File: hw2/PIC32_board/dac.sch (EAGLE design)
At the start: 1 part

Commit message: Edit pin label
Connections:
- net B8/SDI1 renamed A1/SDO1
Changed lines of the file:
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@@
 </segment>
 </net>
-<net name="B8/SDI1" class="0">
+<net name="A1/SDO1" class="0">
 <segment>
 <pinref part="DAC" gate="G$1" pin="5.SDI"/>

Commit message: Add expander chip to schematic library
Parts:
- added 330: (no value), me433:R-US_R0603
- added BUTTON: PUSH, me433:PUSH
- added EXPANDER: MCP23008, me433:MCP23008
- added LED: YELLOW, me433:LED-RED0603
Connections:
- removed net 3.3V: DAC.11.VREFB, DAC.13.VREFA
- new net B2/SDA2: EXPANDER.2.SDA
- new net B3/SCL2: EXPANDER.1.SCL
- new net MCLR: EXPANDER.6.RESET
- new net N$1: EXPANDER.10.GP0, LED.A
- new net N$2: BUTTON.1, EXPANDER.17.GP7
- new net N$3: EXPANDER.3.A2
- new net N$4: EXPANDER.4.A1
- new net N$5: EXPANDER.5.A0
- new net N$6: 330.1, LED.C
- net +3V3: now also DAC.11.VREFB, DAC.13.VREFA, EXPANDER.18.VDD
- net GND: now also 330.2, BUTTON.2, EXPANDER.9.VSS
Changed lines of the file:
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@@
 <part name="GND1" library="me433" deviceset="GND" device=""/>
 <part name="+3V1" library="me433" deviceset="+3V3" device=""/>
+<part name="EXPANDER" library="me433" deviceset="MCP23008" device=""/>
+<part name="+3V2" library="me433" deviceset="+3V3" device=""/>
+<part name="GND2" library="me433" deviceset="GND" device=""/>
+<part name="LED" library="me433" deviceset="LED-RED" device="0603" value="YELLOW"/>
+<part name="GND3" library="me433" deviceset="GND" device=""/>
+<part name="BUTTON" library="me433" deviceset="PUSH" device=""/>
+<part name="GND4" library="me433" deviceset="GND" device=""/>
+<part name="330" library="me433" deviceset="R-US_" device="R0603" package3d_urn="urn:adsk.eagle:package:26057/1"/>
 </parts>
 <sheets>
@@
 <instance part="DAC" gate="G$1" x="-2.54" y="0"/>
 <instance part="GND1" gate="1" x="33.02" y="-20.32"/>
-<instance part="+3V1" gate="G$1" x="-35.56" y="20.32"/>
+<instance part="+3V1" gate="G$1" x="-33.02" y="20.32"/>
 </instances>
 <busses>
 </busses>
 <nets>
-<net name="3.3V" class="0">
-<segment>
-<pinref part="DAC" gate="G$1" pin="13.VREFA"/>
-<wire x1="17.78" y1="10.16" x2="30.48" y2="10.16" width="0.1524" layer="91"/>
-<label x="25.4" y="10.16" size="1.778" layer="95"/>
-</segment>
-<segment>
-<pinref part="DAC" gate="G$1" pin="11.VREFB"/>
-<wire x1="17.78" y1="0" x2="30.48" y2="0" width="0.1524" layer="91"/>
-<label x="25.4" y="0" size="1.778" layer="95"/>
-</segment>
-</net>
 <net name="A0/SS1" class="0">
 <segment>
@@
 <segment>
 <pinref part="DAC" gate="G$1" pin="1.VDD"/>
-<wire x1="-17.78" y1="15.24" x2="-35.56" y2="15.24" width="0.1524" layer="91"/>
-<label x="-33.02" y="15.24" size="1.778" layer="95"/>
+<wire x1="-17.78" y1="15.24" x2="-33.02" y2="15.24" width="0.1524" layer="91"/>
 <pinref part="+3V1" gate="G$1" pin="+3V3"/>
-<wire x1="-35.56" y1="15.24" x2="-35.56" y2="17.78" width="0.1524" layer="91"/>
+<wire x1="-33.02" y1="15.24" x2="-33.02" y2="17.78" width="0.1524" layer="91"/>
+</segment>
+<segment>
+<pinref part="DAC" gate="G$1" pin="13.VREFA"/>
+<wire x1="17.78" y1="10.16" x2="30.48" y2="10.16" width="0.1524" layer="91"/>
+<label x="25.4" y="10.16" size="1.778" layer="95"/>
+</segment>
+<segment>
+<pinref part="DAC" gate="G$1" pin="11.VREFB"/>
+<wire x1="17.78" y1="0" x2="30.48" y2="0" width="0.1524" layer="91"/>
+<label x="25.4" y="0" size="1.778" layer="95"/>
+</segment>
+</net>
+</nets>
+</sheet>
+<sheet>
+<plain>
+</plain>
+<instances>
+<instance part="EXPANDER" gate="G$1" x="0" y="0"/>
+<instance part="+3V2" gate="G$1" x="27.94" y="20.32"/>
+<instance part="GND2" gate="1" x="-27.94" y="-33.02"/>
+<instance part="LED" gate="G$1" x="27.94" y="-25.4" rot="R90"/>
+<instance part="GND3" gate="1" x="48.26" y="-27.94"/>
+<instance part="BUTTON" gate="G$1" x="35.56" y="0" rot="R270"/>
+<instance part="GND4" gate="1" x="35.56" y="-15.24"/>
+<instance part="330" gate="G$1" x="40.64" y="-25.4"/>
+</instances>
+<busses>
+</busses>
+<nets>
+<net name="B3/SCL2" class="0">
+<segment>
+<pinref part="EXPANDER" gate="G$1" pin="1.SCL"/>
+<wire x1="-15.24" y1="15.24" x2="-27.94" y2="15.24" width="0.1524" layer="91"/>
+<label x="-27.94" y="15.24" size="1.778" layer="95"/>
+</segment>
+</net>
+<net name="B2/SDA2" class="0">
+<segment>
+<pinref part="EXPANDER" gate="G$1" pin="2.SDA"/>
+<wire x1="-15.24" y1="10.16" x2="-27.94" y2="10.16" width="0.1524" layer="91"/>
+<label x="-27.94" y="10.16" size="1.778" layer="95"/>
+</segment>
+</net>
+<net name="N$3" class="0">
+<segment>
+<pinref part="EXPANDER" gate="G$1" pin="3.A2"/>
+<wire x1="-15.24" y1="5.08" x2="-27.94" y2="5.08" width="0.1524" layer="91"/>
+</segment>
+</net>
+<net name="N$4" class="0">
+<segment>
+<pinref part="EXPANDER" gate="G$1" pin="4.A1"/>
+<wire x1="-15.24" y1="0" x2="-27.94" y2="0" width="0.1524" layer="91"/>
+</segment>
+</net>
+<net name="N$5" class="0">
+<segment>
+<pinref part="EXPANDER" gate="G$1" pin="5.A0"/>
+<wire x1="-15.24" y1="-5.08" x2="-27.94" y2="-5.08" width="0.1524" layer="91"/>
+</segment>
+</net>
+<net name="MCLR" class="0">
+<segment>
+<pinref part="EXPANDER" gate="G$1" pin="6.RESET"/>
+<wire x1="-15.24" y1="-10.16" x2="-27.94" y2="-10.16" width="0.1524" layer="91"/>
+<label x="-27.94" y="-10.16" size="1.778" layer="95"/>
+</segment>
+</net>
+<net name="+3V3" class="0">
+<segment>
+<pinref part="EXPANDER" gate="G$1" pin="18.VDD"/>
+<wire x1="17.78" y1="15.24" x2="27.94" y2="15.24" width="0.1524" layer="91"/>
+<pinref part="+3V2" gate="G$1" pin="+3V3"/>
+<wire x1="27.94" y1="15.24" x2="27.94" y2="17.78" width="0.1524" layer="91"/>
+</segment>
+</net>
+<net name="GND" class="0">
+<segment>
+<pinref part="EXPANDER" gate="G$1" pin="9.VSS"/>
+<wire x1="-15.24" y1="-25.4" x2="-27.94" y2="-25.4" width="0.1524" layer="91"/>
+<pinref part="GND2" gate="1" pin="GND"/>
+<wire x1="-27.94" y1="-30.48" x2="-27.94" y2="-25.4" width="0.1524" layer="91"/>
+</segment>
+<segment>
+<pinref part="BUTTON" gate="G$1" pin="2"/>
+<pinref part="GND4" gate="1" pin="GND"/>
+<wire x1="35.56" y1="-10.16" x2="35.56" y2="-12.7" width="0.1524" layer="91"/>
+</segment>
+<segment>
+<pinref part="330" gate="G$1" pin="2"/>
+<pinref part="GND3" gate="1" pin="GND"/>
+<wire x1="45.72" y1="-25.4" x2="48.26" y2="-25.4" width="0.1524" layer="91"/>
+</segment>
+</net>
+<net name="N$1" class="0">
+<segment>
+<pinref part="EXPANDER" gate="G$1" pin="10.GP0"/>
+<pinref part="LED" gate="G$1" pin="A"/>
+<wire x1="17.78" y1="-25.4" x2="25.4" y2="-25.4" width="0.1524" layer="91"/>
+</segment>
+</net>
+<net name="N$2" class="0">
+<segment>
+<pinref part="EXPANDER" gate="G$1" pin="17.GP7"/>
+<pinref part="BUTTON" gate="G$1" pin="1"/>
+<wire x1="17.78" y1="10.16" x2="35.56" y2="10.16" width="0.1524" layer="91"/>
+</segment>
+</net>
+<net name="N$6" class="0">
+<segment>
+<pinref part="LED" gate="G$1" pin="C"/>
+<pinref part="330" gate="G$1" pin="1"/>
+<wire x1="33.02" y1="-25.4" x2="35.56" y2="-25.4" width="0.1524" layer="91"/>
 </segment>
 </net>
@@
 </schematic>
 </drawing>
+<compatibility>
+<note version="8.3" severity="warning">
+Since Version 8.3, EAGLE supports URNs for individual library
+assets (packages, symbols, and devices). The URNs of those assets
+will not be understood (or retained) with this version.
+</note>
+<note version="8.3" severity="warning">
+Since Version 8.3, EAGLE supports the association of 3D packages
+with devices in libraries, schematics, and board files. Those 3D
+packages will not be understood (or retained) with this version.
+</note>
+</compatibility>
 </eagle>

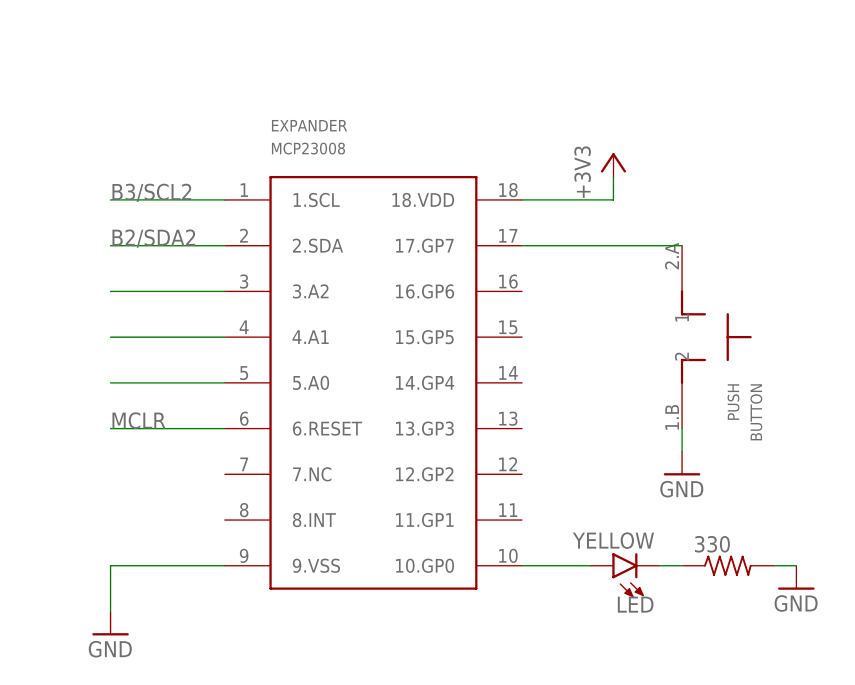
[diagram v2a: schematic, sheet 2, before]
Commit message: Edit schematic labels
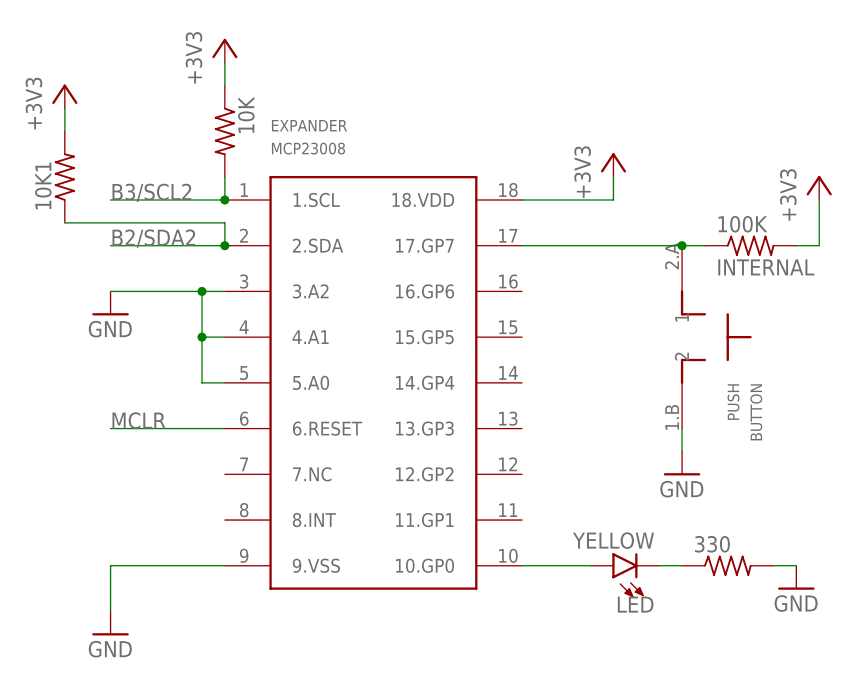
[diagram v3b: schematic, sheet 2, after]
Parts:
- added 100K: INTERNAL, me433:R-US_R0603
- added 10K, 10K1: (no value), me433:R-US_R0603
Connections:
- removed net N$3: EXPANDER.3.A2
- removed net N$4: EXPANDER.4.A1
- removed net N$5: EXPANDER.5.A0
- net +3V3: now also 100K.2, 10K.1, 10K1.2
- net B2/SDA2: now also 10K1.1
- net B3/SCL2: now also 10K.2
- net GND: now also EXPANDER.3.A2, EXPANDER.4.A1, EXPANDER.5.A0
- net N$2: now also 100K.1
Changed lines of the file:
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@@
 <part name="GND4" library="me433" deviceset="GND" device=""/>
 <part name="330" library="me433" deviceset="R-US_" device="R0603" package3d_urn="urn:adsk.eagle:package:26057/1"/>
+<part name="100K" library="me433" deviceset="R-US_" device="R0603" package3d_urn="urn:adsk.eagle:package:26057/1" value="INTERNAL"/>
+<part name="GND5" library="me433" deviceset="GND" device=""/>
+<part name="+3V3" library="me433" deviceset="+3V3" device=""/>
+<part name="10K" library="me433" deviceset="R-US_" device="R0603" package3d_urn="urn:adsk.eagle:package:26057/1"/>
+<part name="10K1" library="me433" deviceset="R-US_" device="R0603" package3d_urn="urn:adsk.eagle:package:26057/1"/>
+<part name="+3V4" library="me433" deviceset="+3V3" device=""/>
+<part name="+3V5" library="me433" deviceset="+3V3" device=""/>
 </parts>
 <sheets>
@@
 <instance part="GND4" gate="1" x="35.56" y="-15.24"/>
 <instance part="330" gate="G$1" x="40.64" y="-25.4"/>
+<instance part="100K" gate="G$1" x="43.18" y="10.16"/>
+<instance part="GND5" gate="1" x="-27.94" y="2.54"/>
+<instance part="+3V3" gate="G$1" x="50.8" y="17.78"/>
+<instance part="10K" gate="G$1" x="-15.24" y="22.86" rot="R270"/>
+<instance part="10K1" gate="G$1" x="-33.02" y="17.78" rot="R90"/>
+<instance part="+3V4" gate="G$1" x="-15.24" y="33.02"/>
+<instance part="+3V5" gate="G$1" x="-33.02" y="27.94"/>
 </instances>
 <busses>
@@
 <wire x1="-15.24" y1="15.24" x2="-27.94" y2="15.24" width="0.1524" layer="91"/>
 <label x="-27.94" y="15.24" size="1.778" layer="95"/>
+<pinref part="10K" gate="G$1" pin="2"/>
+<wire x1="-15.24" y1="15.24" x2="-15.24" y2="17.78" width="0.1524" layer="91"/>
+<junction x="-15.24" y="15.24"/>
 </segment>
 </net>
@@
 <wire x1="-15.24" y1="10.16" x2="-27.94" y2="10.16" width="0.1524" layer="91"/>
 <label x="-27.94" y="10.16" size="1.778" layer="95"/>
-</segment>
-</net>
-<net name="N$3" class="0">
-<segment>
-<pinref part="EXPANDER" gate="G$1" pin="3.A2"/>
-<wire x1="-15.24" y1="5.08" x2="-27.94" y2="5.08" width="0.1524" layer="91"/>
-</segment>
-</net>
-<net name="N$4" class="0">
-<segment>
-<pinref part="EXPANDER" gate="G$1" pin="4.A1"/>
-<wire x1="-15.24" y1="0" x2="-27.94" y2="0" width="0.1524" layer="91"/>
-</segment>
-</net>
-<net name="N$5" class="0">
-<segment>
-<pinref part="EXPANDER" gate="G$1" pin="5.A0"/>
-<wire x1="-15.24" y1="-5.08" x2="-27.94" y2="-5.08" width="0.1524" layer="91"/>
+<wire x1="-15.24" y1="10.16" x2="-15.24" y2="12.7" width="0.1524" layer="91"/>
+<junction x="-15.24" y="10.16"/>
+<pinref part="10K1" gate="G$1" pin="1"/>
+<wire x1="-15.24" y1="12.7" x2="-33.02" y2="12.7" width="0.1524" layer="91"/>
 </segment>
 </net>
@@
 <wire x1="27.94" y1="15.24" x2="27.94" y2="17.78" width="0.1524" layer="91"/>
 </segment>
+<segment>
+<pinref part="100K" gate="G$1" pin="2"/>
+<pinref part="+3V3" gate="G$1" pin="+3V3"/>
+<wire x1="48.26" y1="10.16" x2="50.8" y2="10.16" width="0.1524" layer="91"/>
+<wire x1="50.8" y1="10.16" x2="50.8" y2="15.24" width="0.1524" layer="91"/>
+</segment>
+<segment>
+<pinref part="10K1" gate="G$1" pin="2"/>
+<pinref part="+3V5" gate="G$1" pin="+3V3"/>
+<wire x1="-33.02" y1="22.86" x2="-33.02" y2="25.4" width="0.1524" layer="91"/>
+</segment>
+<segment>
+<pinref part="10K" gate="G$1" pin="1"/>
+<pinref part="+3V4" gate="G$1" pin="+3V3"/>
+<wire x1="-15.24" y1="27.94" x2="-15.24" y2="30.48" width="0.1524" layer="91"/>
+</segment>
 </net>
 <net name="GND" class="0">
@@
 <wire x1="45.72" y1="-25.4" x2="48.26" y2="-25.4" width="0.1524" layer="91"/>
 </segment>
+<segment>
+<pinref part="EXPANDER" gate="G$1" pin="3.A2"/>
+<wire x1="-15.24" y1="5.08" x2="-17.78" y2="5.08" width="0.1524" layer="91"/>
+<pinref part="GND5" gate="1" pin="GND"/>
+<pinref part="EXPANDER" gate="G$1" pin="4.A1"/>
+<wire x1="-17.78" y1="5.08" x2="-27.94" y2="5.08" width="0.1524" layer="91"/>
+<wire x1="-15.24" y1="0" x2="-17.78" y2="0" width="0.1524" layer="91"/>
+<wire x1="-17.78" y1="0" x2="-17.78" y2="5.08" width="0.1524" layer="91"/>
+<junction x="-17.78" y="5.08"/>
+<pinref part="EXPANDER" gate="G$1" pin="5.A0"/>
+<wire x1="-15.24" y1="-5.08" x2="-17.78" y2="-5.08" width="0.1524" layer="91"/>
+<wire x1="-17.78" y1="-5.08" x2="-17.78" y2="0" width="0.1524" layer="91"/>
+<junction x="-17.78" y="0"/>
+</segment>
 </net>
 <net name="N$1" class="0">
@@
 </segment>
 </net>
-<net name="N$2" class="0">
-<segment>
-<pinref part="EXPANDER" gate="G$1" pin="17.GP7"/>
-<pinref part="BUTTON" gate="G$1" pin="1"/>
-<wire x1="17.78" y1="10.16" x2="35.56" y2="10.16" width="0.1524" layer="91"/>
-</segment>
-</net>
 <net name="N$6" class="0">
 <segment>
@@
 </segment>
 </net>
+<net name="N$2" class="0">
+<segment>
+<pinref part="100K" gate="G$1" pin="1"/>
+<pinref part="BUTTON" gate="G$1" pin="1"/>
+<wire x1="38.1" y1="10.16" x2="35.56" y2="10.16" width="0.1524" layer="91"/>
+<pinref part="EXPANDER" gate="G$1" pin="17.GP7"/>
+<wire x1="17.78" y1="10.16" x2="35.56" y2="10.16" width="0.1524" layer="91"/>
+<junction x="35.56" y="10.16"/>
+</segment>
+</net>
